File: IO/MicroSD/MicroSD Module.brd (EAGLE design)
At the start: 25.4 x 25.4 mm, 3 parts

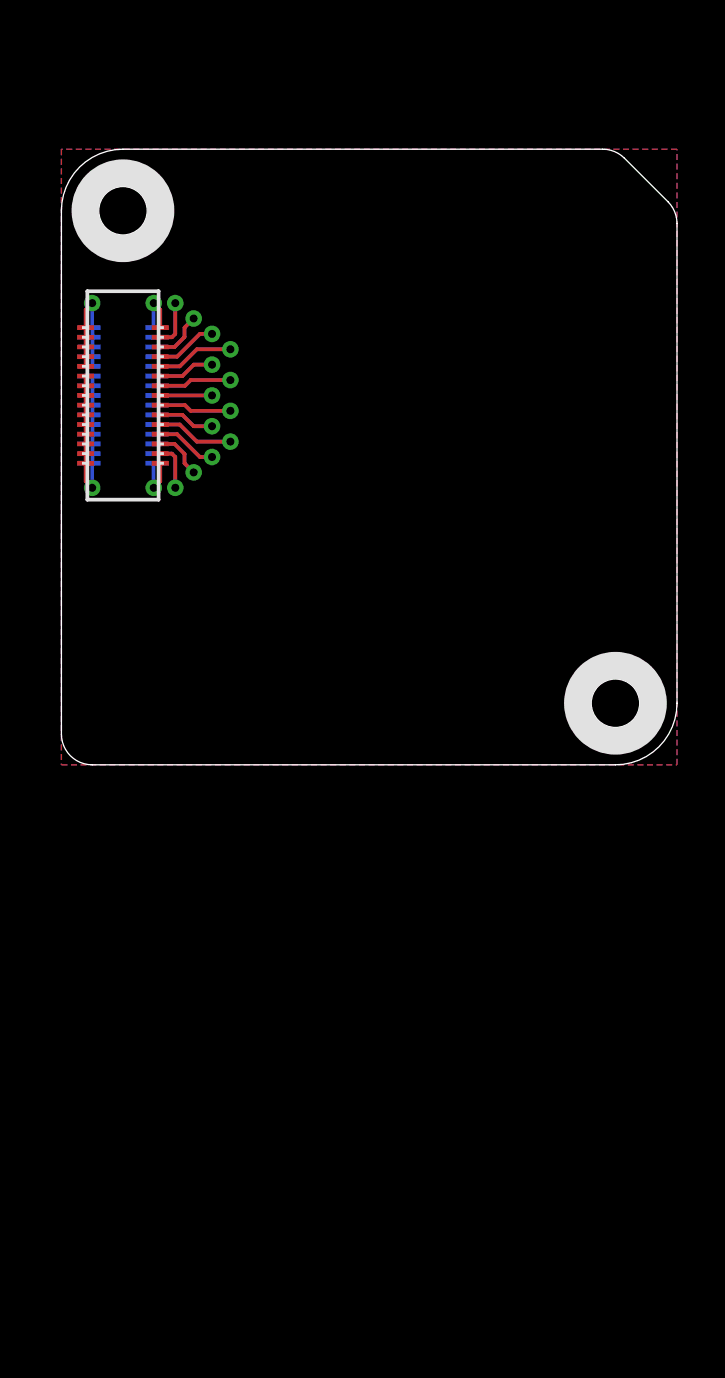
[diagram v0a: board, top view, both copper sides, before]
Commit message: Renamed file to MicroSD Module. Completed Schematic and Board Layout. Needs silkscreen.
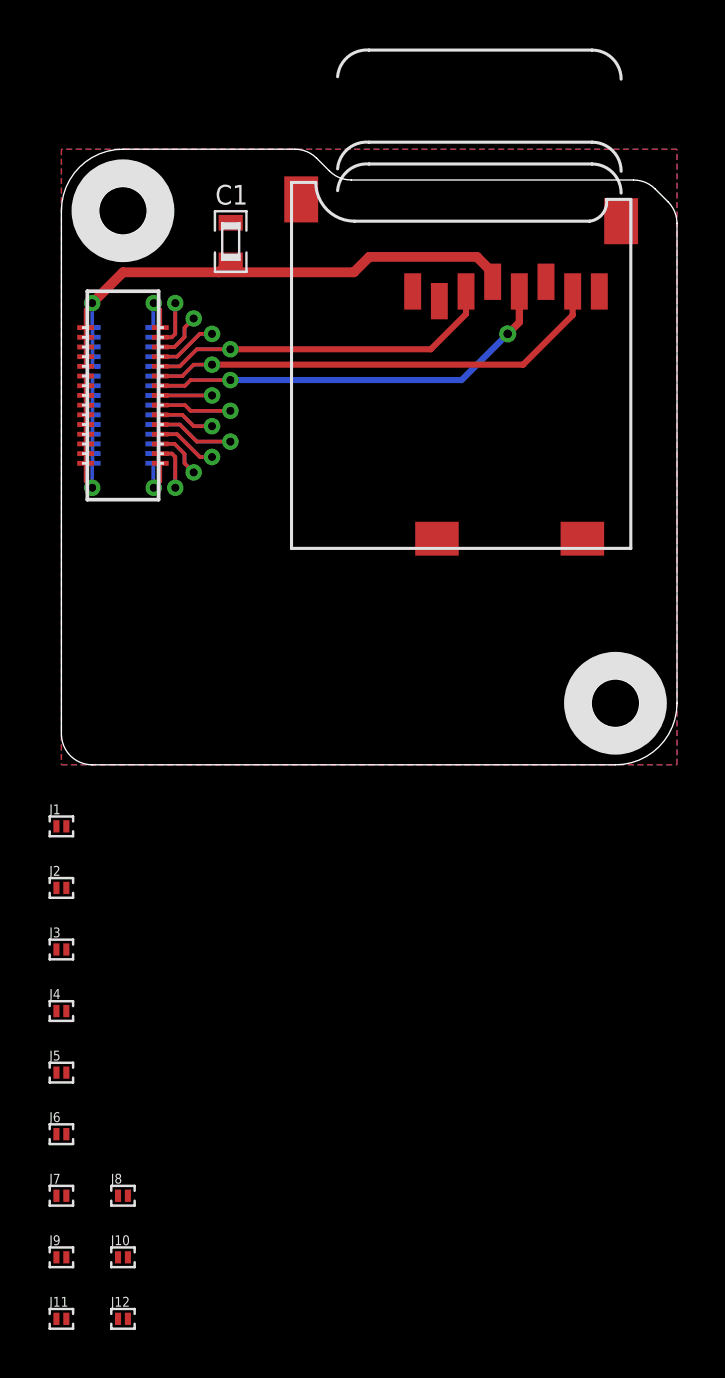
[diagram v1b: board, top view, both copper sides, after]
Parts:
- added C1: .1uF, .standardparts:0603
- added J1, J10, J11, J12, J2, J3, J4, J5, J6, J7, J8, J9: (no value), .solderjumper:2.SML
- added U1: MICROSD, adafruit:MICROSD
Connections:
- removed net N$10: U$8.03, U$8.03@1, U$8.03@VIA
- removed net N$11: U$8.04, U$8.04@1, U$8.04@VIA
- removed net N$12: U$8.05, U$8.05@1, U$8.05@VIA
- removed net N$13: U$8.06, U$8.06@1, U$8.06@VIA
- removed net N$14: U$8.07, U$8.07@1, U$8.07@VIA
- removed net N$15: U$8.WAKE, U$8.WAKE@1, U$8.WAKE@VIA
- removed net N$5 (its old number): U$8.MOSI, U$8.MOSI@1, U$8.MOSI@VIA
- removed net N$6: U$8.MISO, U$8.MISO@1, U$8.MISO@VIA
- removed net N$7: U$8.SCLK, U$8.SCLK@1, U$8.SCLK@VIA
- new net !CS!: J1.2, J2.2, J3.2, J4.2, J5.2, J6.2, U1.2
- new net 01: J7.1
- new net 02: J8.1
- new net 03: J9.1
- new net 04: J10.1
- new net 05: J11.1
- new net 1: J1.1, U$8.03, U$8.03@1, U$8.03@VIA
- new net 2: J2.1, U$8.04, U$8.04@1, U$8.04@VIA
- new net 3: J3.1, U$8.05, U$8.05@1, U$8.05@VIA
- new net 4: J4.1, U$8.06, U$8.06@1, U$8.06@VIA
- new net 5: J5.1, U$8.07, U$8.07@1, U$8.07@VIA
- new net CD: J10.2, J11.2, J12.2, J7.2, J8.2, J9.2, U1.CD1
- new net MISO: U$8.MISO, U$8.MISO@1, U$8.MISO@VIA, U1.7
- new net MOSI: U$8.MOSI, U$8.MOSI@1, U$8.MOSI@VIA, U1.3
- new net SCLK: U$8.SCLK, U$8.SCLK@1, U$8.SCLK@VIA, U1.5
- new net WAKE: J12.1, J6.1, U$8.WAKE, U$8.WAKE@1, U$8.WAKE@VIA
- net 3.3V: now also C1.1, U1.4
- net GND: now also C1.2, U1.6, U1.MT1, U1.MT2
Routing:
- net 3.3V: track 0.00 -> 18.7 mm
- net MISO: track 0.00 -> 16.7 mm
- net SCLK: track 0.00 -> 14.2 mm, vias 0 -> 1
- net MOSI: track 0.00 -> 11.3 mm
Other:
- outline, holes or cut-outs redrawn

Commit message: Completed uSD Module
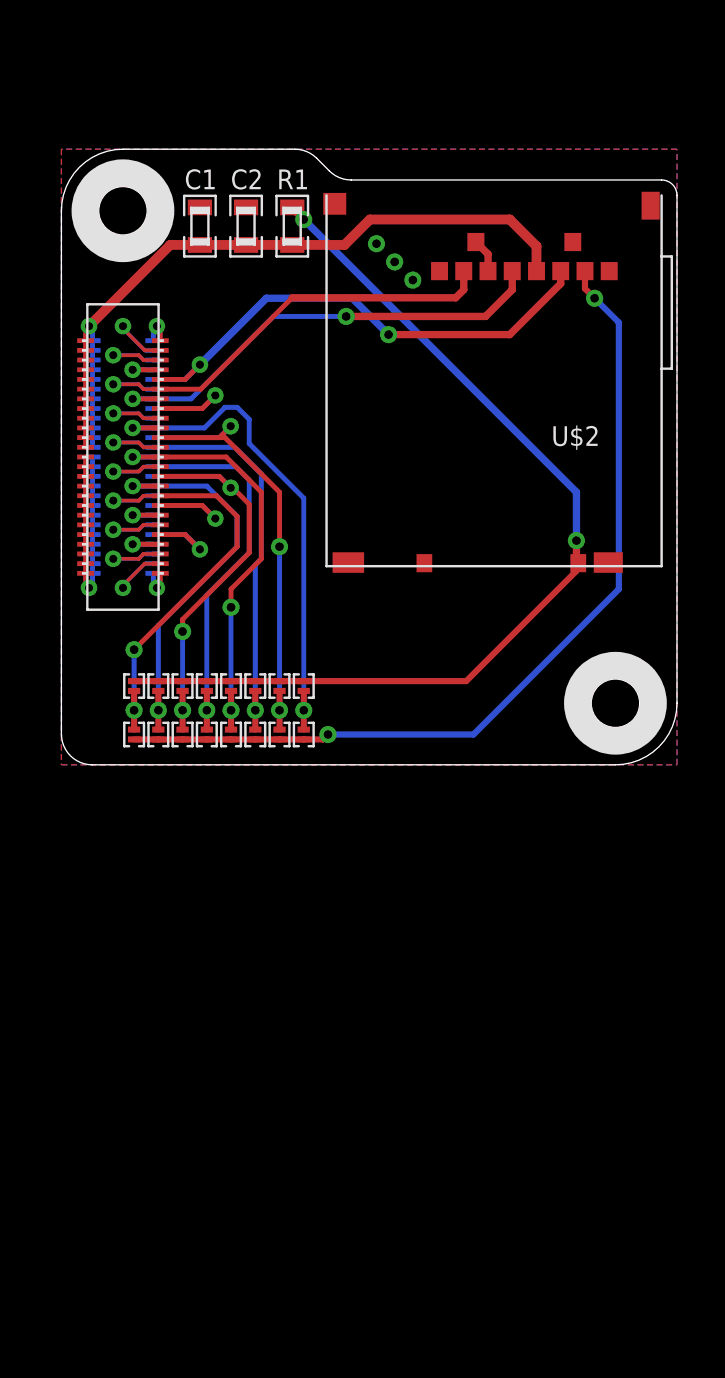
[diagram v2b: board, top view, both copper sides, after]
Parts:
- removed U1: MICROSD, adafruit:MICROSD
- added C2: 1uF, .standardparts:0603
- added J13, J14, J15, J16: (no value), .solderjumper:2.SML
- added R1: 100k, .standardparts:0603
- added U$2: SCHA4B0400, alps:SCHA4B0400
- moved J11 27.3 mm to (8.00, 3.25), turned to 90 degrees
- moved J12 26.5 mm to (7.00, 3.25), turned to 90 degrees
- moved J9 25.6 mm to (10.0, 3.25), turned to 90 degrees
- moved J10 24.4 mm to (9.00, 3.25), turned to 90 degrees
- moved J7 19.4 mm to (4.00, 1.25), turned to 270 degrees
- moved J8 19.0 mm to (3.00, 1.25), turned to 270 degrees
- moved J6 17.2 mm to (5.00, 1.25), turned to 270 degrees
- moved J5 15.2 mm to (6.00, 1.25), turned to 270 degrees
- moved J4 13.4 mm to (7.00, 1.25), turned to 270 degrees
- moved J3 11.9 mm to (8.00, 1.25), turned to 270 degrees
- moved J2 11.0 mm to (9.00, 1.25), turned to 270 degrees
- moved J1 10.7 mm to (10.0, 1.25), turned to 270 degrees
- moved C1 1.42 mm to (5.71, 22.2)
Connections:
- removed net 1: J1.1, U$8.03, U$8.03@1, U$8.03@VIA
- removed net 2: J2.1, U$8.04, U$8.04@1, U$8.04@VIA
- removed net 3: J3.1, U$8.05, U$8.05@1, U$8.05@VIA
- removed net 4: J4.1, U$8.06, U$8.06@1, U$8.06@VIA
- removed net 5: J5.1, U$8.07, U$8.07@1, U$8.07@VIA
- new net 06: J14.1, J6.1, U$8.06, U$8.06@1, U$8.06@VIA
- new net 07: J15.1, J7.1, U$8.07, U$8.07@1, U$8.07@VIA
- new net N$10: U$8.TDO, U$8.TDO@1, U$8.TDO@VIA
- new net N$11: U$8.TCK, U$8.TCK@1, U$8.TCK@VIA
- new net N$12: U$8.TMS, U$8.TMS@1, U$8.TMS@VIA
- new net N$13: U$8.TRST, U$8.TRST@1, U$8.TRST@VIA
- new net N$14: U$8.RST, U$8.RST@1, U$8.RST@VIA
- new net N$6: U$8.TXO.DBG, U$8.TXO.DBG@1, U$8.TXO.DBG@VIA
- new net N$7: U$8.RXI.DBG, U$8.RXI.DBG@1, U$8.RXI.DBG@VIA
- new net N$9: U$8.TDI, U$8.TDI@1, U$8.TDI@VIA
- net !CS!: now also J7.2, J8.2, U$2.!CS!/NC/DAT3; no longer U1.2
- net 01: now also J1.1, J9.1, U$8.01, U$8.01@1, U$8.01@VIA; no longer J7.1
- net 02: now also J10.1, J2.1, U$8.02, U$8.02@1, U$8.02@VIA; no longer J8.1
- net 03: now also J11.1, J3.1, U$8.03, U$8.03@1, U$8.03@VIA; no longer J9.1
- net 04: now also J12.1, J4.1, U$8.04, U$8.04@1, U$8.04@VIA; no longer J10.1
- net 05: now also J13.1, J5.1, U$8.05, U$8.05@1, U$8.05@VIA; no longer J11.1
- net 3.3V: now also C2.1, R1.1, U$2.VDD, U$8.3.3V@11, U$8.3.3V@12, U$8.3.3V@13, U$8.3.3V@14, U$8.3.3V@15, U$8.3.3V@16, U$8.3.3V@17, U$8.3.3V@18, U$8.3.3V@19, U$8.3.3V@20, U$8.3.3V@21, U$8.3.3V@22, U$8.3.3V@23, U$8.3.3V@24; no longer U1.4
- net CD: now also J13.2, J14.2, J15.2, J16.2, R1.2, U$2.CD; no longer J7.2, J8.2, U1.CD1
- net GND: now also C2.2, U$2.GND, U$2.GND@1, U$2.GND@2, U$2.SHIELD, U$2.SHIELD@1, U$2.SHIELD@2, U$2.SHIELD@3, U$2.VSS, U$8.GND@21, U$8.GND@22, U$8.GND@23, U$8.GND@24, U$8.GND@25, U$8.GND@26; no longer U1.6, U1.MT1, U1.MT2
- net MISO: now also U$2.MISO/DAT0; no longer U1.7
- net MOSI: now also U$2.MOSI/CMD; no longer U1.3
- net N$5: now also U$8.RXI, U$8.RXI@1, U$8.RXI@VIA; no longer U$8.02, U$8.02@1, U$8.02@VIA
- net N$8: now also U$8.TXO, U$8.TXO@1, U$8.TXO@VIA; no longer U$8.01, U$8.01@1, U$8.01@VIA
- net SCLK: now also U$2.CLK; no longer U1.5
- net WAKE: now also J16.1, J8.1; no longer J12.1, J6.1
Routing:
- net CD: track 0.00 -> 40.1 mm, vias 0 -> 2
- net !CS!: track 0.00 -> 36.3 mm, vias 0 -> 2
- net 01: track 0.00 -> 19.0 mm, vias 0 -> 1
- net 03: track 0.00 -> 16.4 mm, vias 0 -> 1
- net 05: track 0.00 -> 16.0 mm, vias 0 -> 1
- net 04: track 0.00 -> 15.9 mm, vias 0 -> 2
- net 07: track 0.00 -> 14.9 mm, vias 0 -> 1
- net WAKE: track 0.00 -> 14.9 mm, vias 0 -> 2
- net 02: track 0.00 -> 14.0 mm, vias 0 -> 2
- net 06: track 0.00 -> 12.3 mm, vias 0 -> 2
- net MOSI: track 11.3 -> 18.0 mm, vias 0 -> 1
- net SCLK: track 14.2 -> 17.4 mm
- net 3.3V: track 18.7 -> 21.8 mm
- net MISO: track 16.7 -> 15.0 mm
- net GND: track 0.00 -> 1.41 mm, vias 0 -> 3
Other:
- outline, holes or cut-outs redrawn
- board text added: "!CS"
- board text added: "CD"
- board text added: "Cruz Monrreal II"
- board text added: "InnovativeMaker.com"
- board text added: "v1"
